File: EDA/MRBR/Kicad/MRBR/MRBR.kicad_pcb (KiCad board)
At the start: 2 copper layers, 24 parts, among them J1 TYPE-C-31-M-12, Q1 MMBT489LT1G, Q2 MMBT489LT1G, SW1 Reset, U1 ESP32-WROOM-32, U2 NCP1117ST33T3G, U3 FT232RL

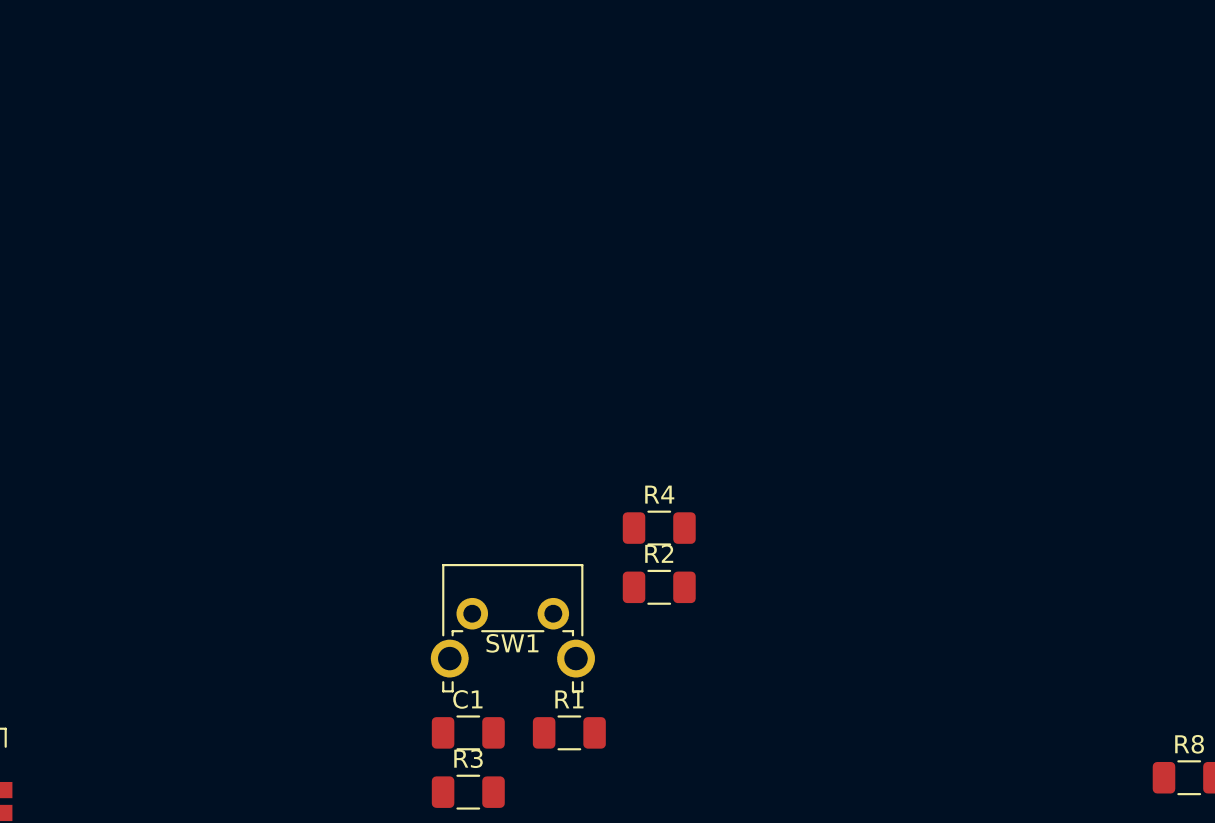
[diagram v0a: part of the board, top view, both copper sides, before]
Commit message: Added barrel jack to PSU
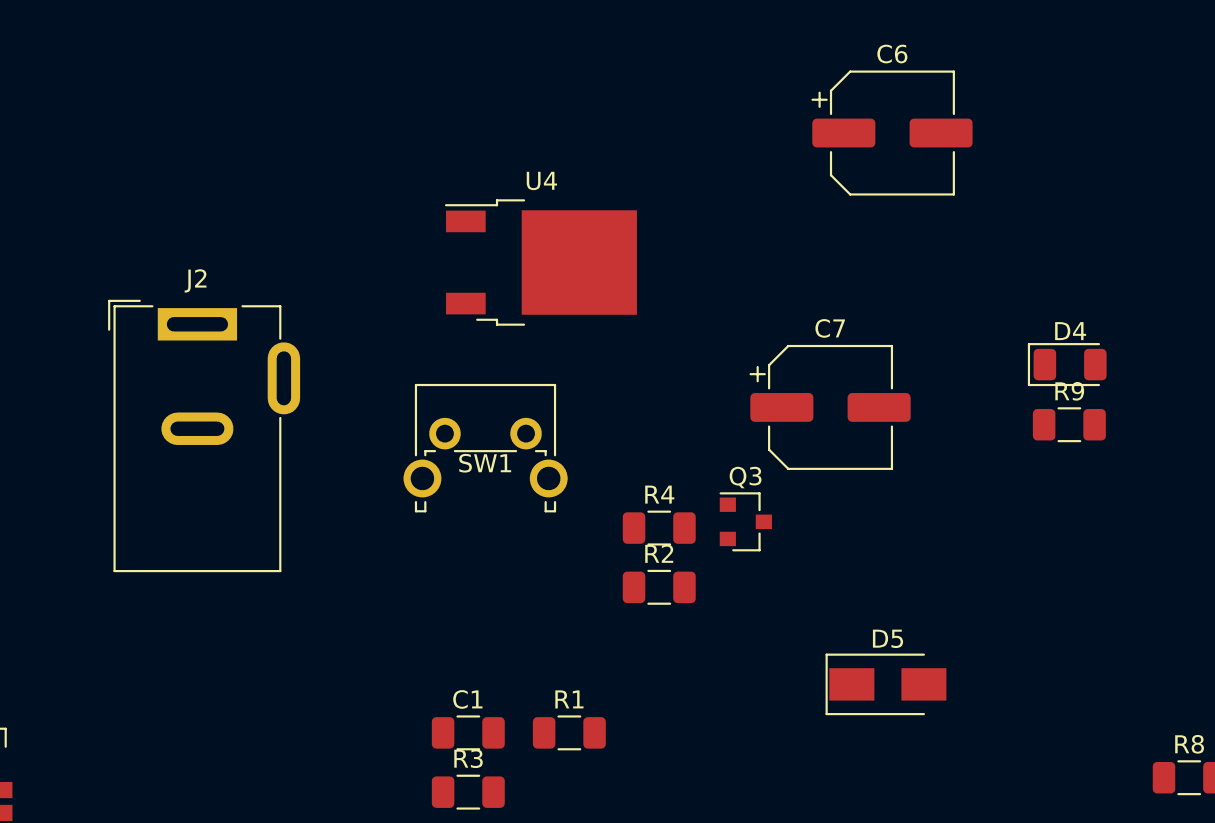
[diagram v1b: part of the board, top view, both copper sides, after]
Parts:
- added C6: 47uF, Capacitor_SMD:CP_Elec_6.3x7.7, F.Cu at (142.9, 31.5)
- added C7: 47uF, Capacitor_SMD:CP_Elec_6.3x7.7, F.Cu at (139.5, 46.7)
- added D4: BT_LED, LED_SMD:LED_1206_3216Metric, F.Cu at (152.8, 44.3)
- added D5: M7, Diode_SMD:D_SMA, F.Cu at (142.7, 62.1)
- added J2: Barrel_Jack_Switch_Pin3Ring, Connector_BarrelJack:BarrelJack_Wuerth_6941xx301002, F.Cu at (104.3, 42.1)
- added Q3: FDN340P, Package_TO_SOT_SMD:SOT-23, F.Cu at (134.8, 53.1)
- added R9: 220R, Resistor_SMD:R_1206_3216Metric, F.Cu at (152.7, 47.7)
- added U4: MC33269DT-5.0G, Package_TO_SOT_SMD:TO-252-2, F.Cu at (123.4, 38.7)
- moved SW1 10.1 mm to (118.1, 48.2)
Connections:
- net Net-(U1-Pad17) renamed /SD2_NC
- net Net-(U1-Pad18) renamed /SD3_NC
- net Net-(U1-Pad19) renamed /CMD_NC
- net Net-(U1-Pad20) renamed /CLK_NC
- net Net-(U1-Pad21) renamed /SD0_NC
- net Net-(U1-Pad22) renamed /SD1_NC
- net Net-(U1-Pad4) renamed /S_VP_NC
- net Net-(U1-Pad5) renamed /S_VN_NC
- C2 pad 1: VBUS -> +5V
- U2 pad 3: VBUS -> +5V
- U3 pad 20: VBUS -> +5V
